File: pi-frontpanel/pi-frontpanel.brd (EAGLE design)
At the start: 105.4 x 66 mm, 15 parts

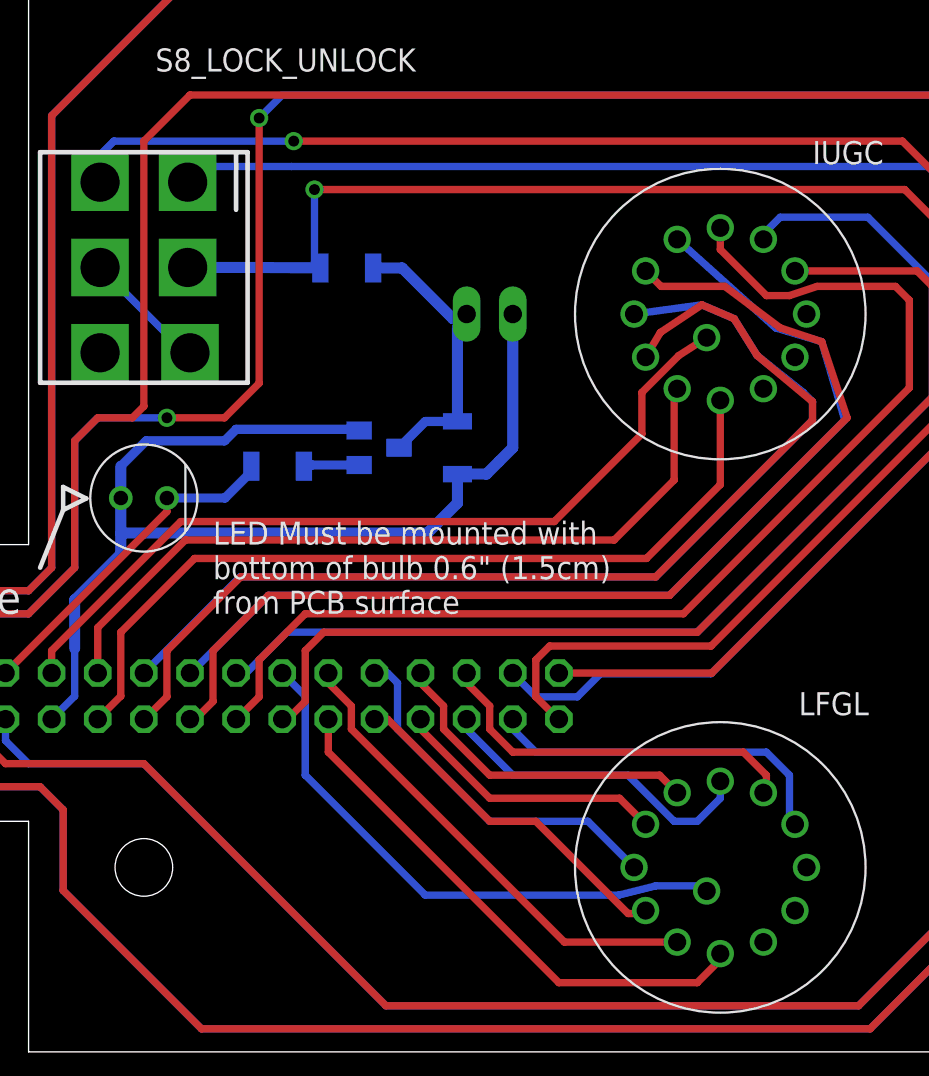
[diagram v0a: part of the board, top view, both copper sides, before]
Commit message: Calibration Windows
I've opened up windows above POT1-3 and U9, pin 10. The windows allow access to the pots and U9 for initial calibration of the PI controller.

DSB
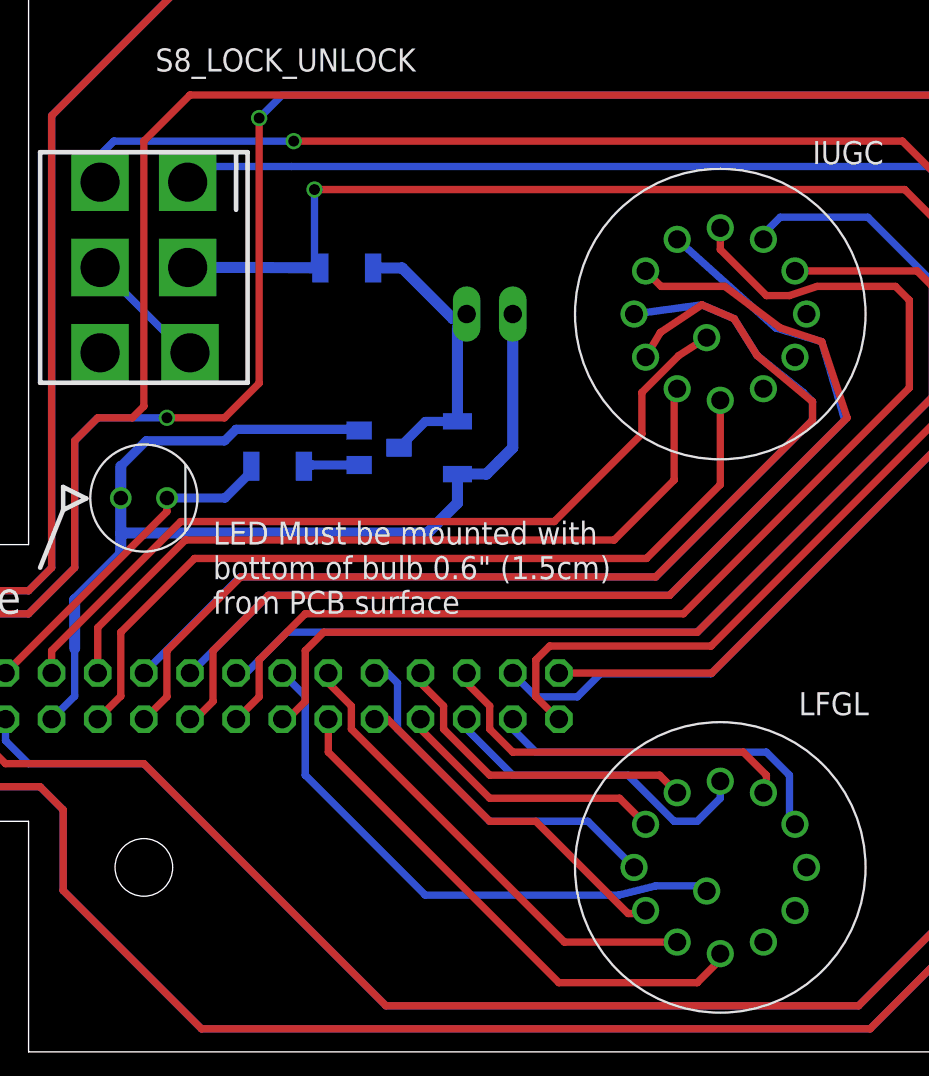
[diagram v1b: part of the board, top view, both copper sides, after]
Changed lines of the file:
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@@
 <?xml version="1.0" encoding="utf-8"?>
 <!DOCTYPE eagle SYSTEM "eagle.dtd">
-<eagle version="6.6.0">
+<eagle version="9.3.0">
 <drawing>
 <settings>
-<setting alwaysvectorfont="yes"/>
+<setting alwaysvectorfont="no"/>
+<setting keepoldvectorfont="yes"/>
 <setting verticaltext="up"/>
 </settings>
@@
 </class>
 </classes>
-<designrules name="default">
-<description language="de">&lt;b&gt;EAGLE Design Rules&lt;/b&gt;
-&lt;p&gt;
-Die Standard-Design-Rules sind so gewählt, dass sie für
-die meisten Anwendungen passen. Sollte ihre Platine
-besondere Anforderungen haben, treffen Sie die erforderlichen
-Einstellungen hier und speichern die Design Rules unter
-einem neuen Namen ab.</description>
-<description language="en">&lt;b&gt;EAGLE Design Rules&lt;/b&gt;
-&lt;p&gt;
-The default Design Rules have been set to cover
-a wide range of applications. Your particular design
-may have different requirements, so please make the
-necessary adjustments and save your customized
-design rules under a new name.</description>
+<designrules name="MF_Standard_2_Layer">
+<description language="en">&lt;b&gt;MacroFab, INC. EAGLE Design Rules&lt;/b&gt;
+&lt;p&gt;This DRC check is for 2-Layer Standard Capability boards to be manufactured through the MacroFab, INC. service.</description>
 <param name="layerSetup" value="(1*16)"/>
-<param name="mtCopper" value="0.035mm 0.035mm 0.035mm 0.035mm 0.035mm 0.035mm 0.035mm 0.035mm 0.035mm 0.035mm 0.035mm 0.035mm 0.035mm 0.035mm 0.035mm 0.035mm"/>
-<param name="mtIsolate" value="1.5mm 0.15mm 0.2mm 0.15mm 0.2mm 0.15mm 0.2mm 0.15mm 0.2mm 0.15mm 0.2mm 0.15mm 0.2mm 0.15mm 0.2mm"/>
-<param name="mdWireWire" value="8mil"/>
-<param name="mdWirePad" value="8mil"/>
-<param name="mdWireVia" value="8mil"/>
-<param name="mdPadPad" value="8mil"/>
-<param name="mdPadVia" value="8mil"/>
-<param name="mdViaVia" value="8mil"/>
-<param name="mdSmdPad" value="8mil"/>
-<param name="mdSmdVia" value="8mil"/>
-<param name="mdSmdSmd" value="8mil"/>
+<param name="mtCopper" value="0.035mm 0.0175mm 0.035mm 0.035mm 0.035mm 0.035mm 0.035mm 0.035mm 0.035mm 0.035mm 0.035mm 0.035mm 0.035mm 0.035mm 0.0175mm 0.035mm"/>
+<param name="mtIsolate" value="1.5mm 1.1mm 0.2mm 0.15mm 0.2mm 0.15mm 0.2mm 0.15mm 0.2mm 0.15mm 0.2mm 0.15mm 0.2mm 0.15mm 0.2mm"/>
+<param name="mdWireWire" value="5mil"/>
+<param name="mdWirePad" value="5mil"/>
+<param name="mdWireVia" value="5mil"/>
+<param name="mdPadPad" value="5mil"/>
+<param name="mdPadVia" value="5mil"/>
+<param name="mdViaVia" value="5mil"/>
+<param name="mdSmdPad" value="0mil"/>
+<param name="mdSmdVia" value="0mil"/>
+<param name="mdSmdSmd" value="0mil"/>
 <param name="mdViaViaSameLayer" value="8mil"/>
 <param name="mnLayersViaInSmd" value="2"/>
-<param name="mdCopperDimension" value="40mil"/>
-<param name="mdDrill" value="8mil"/>
+<param name="mdCopperDimension" value="10mil"/>
+<param name="mdDrill" value="10mil"/>
 <param name="mdSmdStop" value="0mil"/>
-<param name="msWidth" value="10mil"/>
-<param name="msDrill" value="24mil"/>
-<param name="msMicroVia" value="9.99mm"/>
+<param name="msWidth" value="5mil"/>
+<param name="msDrill" value="10mil"/>
+<param name="msMicroVia" value="10mil"/>
 <param name="msBlindViaRatio" value="0.5"/>
 <param name="rvPadTop" value="0.25"/>
@@
 <param name="rvMicroViaOuter" value="0.25"/>
 <param name="rvMicroViaInner" value="0.25"/>
-<param name="rlMinPadTop" value="10mil"/>
+<param name="rlMinPadTop" value="4mil"/>
 <param name="rlMaxPadTop" value="20mil"/>
-<param name="rlMinPadInner" value="10mil"/>
+<param name="rlMinPadInner" value="4mil"/>
 <param name="rlMaxPadInner" value="20mil"/>
-<param name="rlMinPadBottom" value="10mil"/>
+<param name="rlMinPadBottom" value="4mil"/>
 <param name="rlMaxPadBottom" value="20mil"/>
-<param name="rlMinViaOuter" value="8mil"/>
+<param name="rlMinViaOuter" value="4mil"/>
 <param name="rlMaxViaOuter" value="20mil"/>
-<param name="rlMinViaInner" value="8mil"/>
+<param name="rlMinViaInner" value="4mil"/>
 <param name="rlMaxViaInner" value="20mil"/>
 <param name="rlMinMicroViaOuter" value="4mil"/>
@@
 <param name="psTop" value="-1"/>
 <param name="psBottom" value="-1"/>
-<param name="psFirst" value="-1"/>
+<param name="psFirst" value="0"/>
 <param name="psElongationLong" value="100"/>
 <param name="psElongationOffset" value="100"/>
 <param name="mvStopFrame" value="1"/>
 <param name="mvCreamFrame" value="0"/>
-<param name="mlMinStopFrame" value="4mil"/>
-<param name="mlMaxStopFrame" value="4mil"/>
+<param name="mlMinStopFrame" value="2mil"/>
+<param name="mlMaxStopFrame" value="2mil"/>
 <param name="mlMinCreamFrame" value="0mil"/>
 <param name="mlMaxCreamFrame" value="0mil"/>
-<param name="mlViaStopLimit" value="0mil"/>
+<param name="mlViaStopLimit" value="25mil"/>
 <param name="srRoundness" value="0"/>
 <param name="srMinRoundness" value="0mil"/>
@@
 <param name="dpMaxLengthDifference" value="10mm"/>
 <param name="dpGapFactor" value="2.5"/>
-<param name="checkGrid" value="0"/>
 <param name="checkAngle" value="0"/>
 <param name="checkFont" value="1"/>
-<param name="checkRestrict" value="1"/>
+<param name="checkRestrict" value="0"/>
+<param name="checkStop" value="0"/>
+<param name="checkValues" value="0"/>
+<param name="checkNames" value="1"/>
+<param name="checkWireStubs" value="1"/>
+<param name="checkPolygonWidth" value="0"/>
 <param name="useDiameter" value="13"/>
 <param name="maxErrors" value="50"/>
@@
 <pass name="Default">
 <param name="RoutingGrid" value="50mil"/>
+<param name="AutoGrid" value="1"/>
+<param name="Efforts" value="0"/>
+<param name="TopRouterVariant" value="1"/>
 <param name="tpViaShape" value="round"/>
 <param name="PrefDir.1" value="|"/>
@@
 <attribute name="PARTNO" value="360-2368-ND" x="158.75" y="15.24" size="1.778" layer="27" display="off"/>
 </element>
-<element name="JP1" library="pinhead" package="2X18" value="" x="128.27" y="24.6761" rot="MR0">
+<element name="JP1" library="pinhead" package="2X18" value="" x="128.27" y="24.6761" smashed="yes" rot="MR0">
+<attribute name="NAME" x="151.13" y="27.8511" size="1.27" layer="26" ratio="10" rot="MR0"/>
 <attribute name="PARTNO" value="S7086-ND" x="128.27" y="24.6761" size="1.778" layer="28" rot="MR0" display="off"/>
+<attribute name="VALUE" x="151.13" y="20.2311" size="1.27" layer="28" rot="MR0"/>
 </element>
 <element name="IN_MON" library="connector-jqi" package="BNC-V" value="BNC-V" x="184.15" y="48.26" smashed="yes">
@@
 </element>
 <element name="S8_LOCK_UNLOCK" library="pi-frontpanel" package="SP3T_LUG" value="" x="127" y="48.2854" smashed="yes">
+<attribute name="NAME" x="127.635" y="59.0804" size="1.27" layer="21"/>
 <attribute name="PARTNUM" value="450-1536-ND" x="127" y="48.2854" size="1.778" layer="27" display="off"/>
-<attribute name="NAME" x="127.635" y="59.0804" size="1.27" layer="21"/>
 </element>
 <element name="S7_MON_IN_SEL" library="pi-frontpanel" package="SPDT_LUG" value="SPDT" x="184.15" y="63.5" smashed="yes" rot="R90">
@@
 <attribute name="PARTNO" value="67-2207-ND" x="127" y="35.5854" size="1.778" layer="27" display="off"/>
 </element>
-<element name="R1" library="jqi_passives" package="R_1206" value="14k" x="138.176" y="48.26" rot="MR0">
+<element name="R1" library="jqi_passives" package="R_1206" value="14k" x="138.176" y="48.26" smashed="yes" rot="MR0">
+<attribute name="NAME" x="140.176" y="49.46" size="1.016" layer="26" font="vector" rot="MR0"/>
 <attribute name="PARTNO" value="P14.0KFCT-ND" x="138.176" y="48.26" size="1.778" layer="28" rot="MR0" display="off"/>
 </element>
-<element name="R2" library="jqi_passives" package="R_1206" value="4.99k" x="144.272" y="38.354" rot="MR90">
+<element name="R2" library="jqi_passives" package="R_1206" value="4.99k" x="144.272" y="38.354" smashed="yes" rot="MR90">
+<attribute name="NAME" x="145.472" y="36.354" size="1.016" layer="26" font="vector" rot="MR90"/>
 <attribute name="PARTNO" value="P4.99KFCT-ND" x="144.272" y="38.354" size="1.778" layer="28" rot="MR90" display="off"/>
 </element>
 <element name="T1" library="transistor" package="SOT23-BEC" value="" x="139.954" y="38.354" smashed="yes" rot="MR90">
+<attribute name="NAME" x="141.097" y="34.925" size="1.27" layer="26" rot="MR0"/>
 <attribute name="PARTNO" value="MMBT2222A-FDICT-ND" x="139.954" y="38.354" size="1.778" layer="28" rot="MR90" display="off"/>
-<attribute name="NAME" x="141.097" y="34.925" size="1.27" layer="26" rot="MR0"/>
 <attribute name="VALUE" x="136.779" y="36.449" size="1.27" layer="28" rot="MR90"/>
 </element>
-<element name="R3" library="jqi_passives" package="R_1206" value="4.99k" x="134.366" y="37.338" rot="MR0">
+<element name="R3" library="jqi_passives" package="R_1206" value="4.99k" x="134.366" y="37.338" smashed="yes" rot="MR0">
+<attribute name="NAME" x="136.366" y="38.538" size="1.016" layer="26" font="vector" rot="MR0"/>
 <attribute name="PARTNO" value="P4.99KFCT-ND" x="134.366" y="37.338" size="1.778" layer="28" rot="MR0" display="off"/>
 </element>
 <element name="JP2" library="pinhead" package="1X02" value="" x="146.05" y="45.72" smashed="yes" rot="MR180">
+<attribute name="NAME" x="144.0688" y="49.6062" size="1.27" layer="26" ratio="10" rot="MR180"/>
 <attribute name="PARTNO" value="A1921-ND" x="146.05" y="45.72" size="1.778" layer="28" rot="MR180" display="off"/>
-<attribute name="NAME" x="144.0688" y="49.6062" size="1.27" layer="26" ratio="10" rot="MR180"/>
 <attribute name="VALUE" x="143.51" y="48.895" size="1.27" layer="28" rot="MR180"/>
 </element>
@@
 </signal>
 </signals>
+<mfgpreviewcolors>
+<mfgpreviewcolor name="soldermaskcolor" color="0xC8008000"/>
+<mfgpreviewcolor name="silkscreencolor" color="0xFFFEFEFE"/>
+<mfgpreviewcolor name="backgroundcolor" color="0xFF282828"/>
+<mfgpreviewcolor name="coppercolor" color="0xFFFFBF00"/>
+<mfgpreviewcolor name="substratecolor" color="0xFF786E46"/>
+</mfgpreviewcolors>
 </board>
 </drawing>
